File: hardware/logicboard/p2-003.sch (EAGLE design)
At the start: 67 parts, among them IC1 74LS06N, IC11 74LS153D, IC12 LTC485S, IC13 LTC485S, IC2 4066N, J1 MKR, J11 Qwiic, J12 Qwiic, J13 Qwiic, J14 Qwiic, J2 GPIO, J3 Vcc, J4 RLY, J5 SPI, J6 LED, K1 G5V1, T1 2SC1815, U1 DS18B20

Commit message: Very rough but should be okay.
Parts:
- removed C11, C12, C13: 10n, rcl:C-EUC2012
- removed IC11: 74LS153D, 74xx-us:74LS153D
- removed IC12, IC13: LTC485S, linear-technology:LTC485S
- removed IN, RX: (no value), wirepad:SMD2
- removed J11, J12, J13, J14: Qwiic, SparkFun-Connectors:QWIIC_CONNECTORJS-1MM
- removed J6: LED, SparkFun-Connectors:CONN_03JST-PTH
- removed JP3: MPXJMP, pinhead:PINHD-1X2
- removed JP5: D5V, pinhead:PINHD-1X3
- removed JP6: LED, pinhead:PINHD-1X3
- removed R11: 10k, rcl:R-EU_M2012
- removed R12, R13: 120, rcl:R-EU_M2012
- removed R3, R4: 120, resistor:R-EU_0204/5
- added J10: (no value), con-jack:JACK-PLUG0
- added J7, J8, J9: DIN5, SparkFun-Connectors:DIN5
- added X3: MKDSN1,5/2-5,08, con-phoenix-508:MKDSN1,5/2-5,08
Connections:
- removed net LED0A: J6.1, JP6.1, R4.1
- removed net LED1A: J6.3, JP6.3, R3.1
- removed net MIN: IC11A.1C1, IN.P, JP3.2, OK1A.VO1
- removed net MRX: IC11A.1C0, IC12.RO
- net GND: now also X3-1.KL; no longer C11.2, C12.2, C13.2, IC11A.1C2, IC11A.1C3, IC11A.1G, IC11A.2C0, IC11A.2C1, IC11A.2C2, IC11A.2C3, IC11A.2G, IC11A.B, IC12.!RE, IC12.DE, IC12.DI, IC12.GND, IC13.GND, J11.GND, J12.GND, J13.GND, J14.GND, J6.2, JP5.1, JP6.2
- net LED0: no longer R4.2
- net LED1: no longer R3.2
- net MRX+: no longer IC12.A, R12.1
- net MRX-: no longer IC12.B, R12.2
- net MRXDTCT: no longer IC11A.A, R11.1
- net MTX+: no longer IC13.A, R13.1
- net MTX-: no longer IC13.B, R13.2
- net RX: now also OK1A.VO1; no longer IC11A.1Y, JP3.1, RX.P
- net SCL: no longer J11.SCL, J12.SCL, J13.SCL, J14.SCL
- net SDA: no longer J11.SDA, J12.SDA, J13.SDA, J14.SDA
- net TX: no longer IC13.DI
- net V+: now also X3-2.KL; no longer JP5.3
- net VCC: no longer C11.1, C12.1, C13.1, IC12.VCC, IC13.!RE, IC13.DE, IC13.VCC, J11.VCC, J12.VCC, J13.VCC, J14.VCC, JP5.2, R11.2

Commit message: Configuring.
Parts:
- added JP3: (no value), pinhead:PINHD-1X3
- added JP5: (no value), pinhead:PINHD-1X2
- added R3, R4: 1k, resistor:R-EU_0204/5
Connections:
- new net LED0A: JP3.3, R3.1
- new net LED1A: JP3.1, R4.1
- net GND: now also JP3.2
- net LED0: now also R3.2
- net LED1: now also R4.2
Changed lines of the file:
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@@
 <part name="J10" library="con-jack" library_urn="urn:adsk.eagle:library:154" deviceset="JACK-PLUG" device="0" package3d_urn="urn:adsk.eagle:package:7492/1"/>
 <part name="X3" library="con-phoenix-508" library_urn="urn:adsk.eagle:library:176" deviceset="MKDSN1,5/2-5,08" device="" package3d_urn="urn:adsk.eagle:package:9630/1"/>
+<part name="R3" library="resistor" library_urn="urn:adsk.eagle:library:348" deviceset="R-EU_" device="0204/5" package3d_urn="urn:adsk.eagle:package:23488/1" value="1k"/>
+<part name="R4" library="resistor" library_urn="urn:adsk.eagle:library:348" deviceset="R-EU_" device="0204/5" package3d_urn="urn:adsk.eagle:package:23488/1" value="1k"/>
+<part name="JP3" library="pinhead" library_urn="urn:adsk.eagle:library:325" deviceset="PINHD-1X3" device="" package3d_urn="urn:adsk.eagle:package:22458/2"/>
+<part name="JP5" library="pinhead" library_urn="urn:adsk.eagle:library:325" deviceset="PINHD-1X2" device="" package3d_urn="urn:adsk.eagle:package:22435/2"/>
 </parts>
 <sheets>
@@
 <attribute name="VALUE" x="342.9" y="49.657" size="1.778" layer="96" rot="MR0"/>
 </instance>
+<instance part="R3" gate="G$1" x="93.98" y="33.02" smashed="yes">
+<attribute name="NAME" x="93.98" y="35.56" size="1.778" layer="95" align="bottom-center"/>
+<attribute name="VALUE" x="93.98" y="30.48" size="1.778" layer="96" align="top-center"/>
+</instance>
+<instance part="R4" gate="G$1" x="93.98" y="38.1" smashed="yes">
+<attribute name="NAME" x="93.98" y="40.64" size="1.778" layer="95" align="bottom-center"/>
+<attribute name="VALUE" x="93.98" y="35.56" size="1.778" layer="96" align="top-center"/>
+</instance>
+<instance part="JP3" gate="A" x="71.12" y="35.56" smashed="yes" rot="MR0">
+<attribute name="NAME" x="77.47" y="41.275" size="1.778" layer="95" rot="MR0"/>
+<attribute name="VALUE" x="77.47" y="27.94" size="1.778" layer="96" rot="MR0"/>
+</instance>
+<instance part="JP5" gate="G$1" x="30.48" y="165.1" smashed="yes" rot="MR0">
+<attribute name="NAME" x="36.83" y="170.815" size="1.778" layer="95" rot="MR0"/>
+<attribute name="VALUE" x="36.83" y="160.02" size="1.778" layer="96" rot="MR0"/>
+</instance>
 </instances>
 <busses>
@@
 <junction x="78.74" y="35.56"/>
 <wire x1="78.74" y1="20.32" x2="66.04" y2="20.32" width="0.1524" layer="91"/>
+<pinref part="JP3" gate="A" pin="2"/>
 </segment>
 <segment>
@@
 <wire x1="312.42" y1="91.44" x2="309.88" y2="91.44" width="0.1524" layer="91"/>
 <label x="309.88" y="91.44" size="0.8128" layer="95" rot="MR0" xref="yes"/>
-</segment>
-<segment>
-<wire x1="35.56" y1="162.56" x2="43.18" y2="162.56" width="0.1524" layer="91"/>
-<label x="43.18" y="162.56" size="0.8128" layer="95" xref="yes"/>
 </segment>
 <segment>
@@
 </segment>
 <segment>
-<wire x1="35.56" y1="165.1" x2="43.18" y2="165.1" width="0.1524" layer="91"/>
-<label x="43.18" y="165.1" size="0.8128" layer="95" xref="yes"/>
-</segment>
-<segment>
 <wire x1="96.52" y1="66.04" x2="101.6" y2="66.04" width="0.1524" layer="91"/>
 <pinref part="J3" gate="G$1" pin="2"/>
@@
 <wire x1="99.06" y1="33.02" x2="101.6" y2="33.02" width="0.1524" layer="91"/>
 <label x="101.6" y="33.02" size="0.8128" layer="95" xref="yes"/>
+<pinref part="R3" gate="G$1" pin="2"/>
 </segment>
 <segment>
@@
 <wire x1="99.06" y1="38.1" x2="101.6" y2="38.1" width="0.1524" layer="91"/>
 <label x="101.6" y="38.1" size="0.8128" layer="95" xref="yes"/>
+<pinref part="R4" gate="G$1" pin="2"/>
 </segment>
 </net>
@@
 <wire x1="76.2" y1="22.86" x2="66.04" y2="22.86" width="0.1524" layer="91"/>
 <label x="81.28" y="38.1" size="1.778" layer="95"/>
+<pinref part="R4" gate="G$1" pin="1"/>
+<pinref part="JP3" gate="A" pin="1"/>
 </segment>
 </net>
@@
 </segment>
 <segment>
-<wire x1="35.56" y1="167.64" x2="43.18" y2="167.64" width="0.1524" layer="91"/>
-<label x="43.18" y="167.64" size="0.8128" layer="95" xref="yes"/>
-</segment>
-<segment>
 <pinref part="SV2" gate="-2" pin="S"/>
 <wire x1="312.42" y1="157.48" x2="309.88" y2="157.48" width="0.1524" layer="91"/>
@@
 <junction x="81.28" y="33.02"/>
 <label x="81.28" y="33.02" size="1.778" layer="95"/>
-</segment>
-</net>
+<pinref part="R3" gate="G$1" pin="1"/>
+<pinref part="JP3" gate="A" pin="3"/>
+</segment>
+</net>

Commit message: First try. Should work. Need to renumber and rename parts.
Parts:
- removed C10: 100n, rcl:C-EU025-024X044
- removed C8, C9: 10n, resistor:C-EU025-024X044
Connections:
- net GND: no longer C10.2, C8.2, C9.2
- net VCC: no longer C10.1, C8.1, C9.1

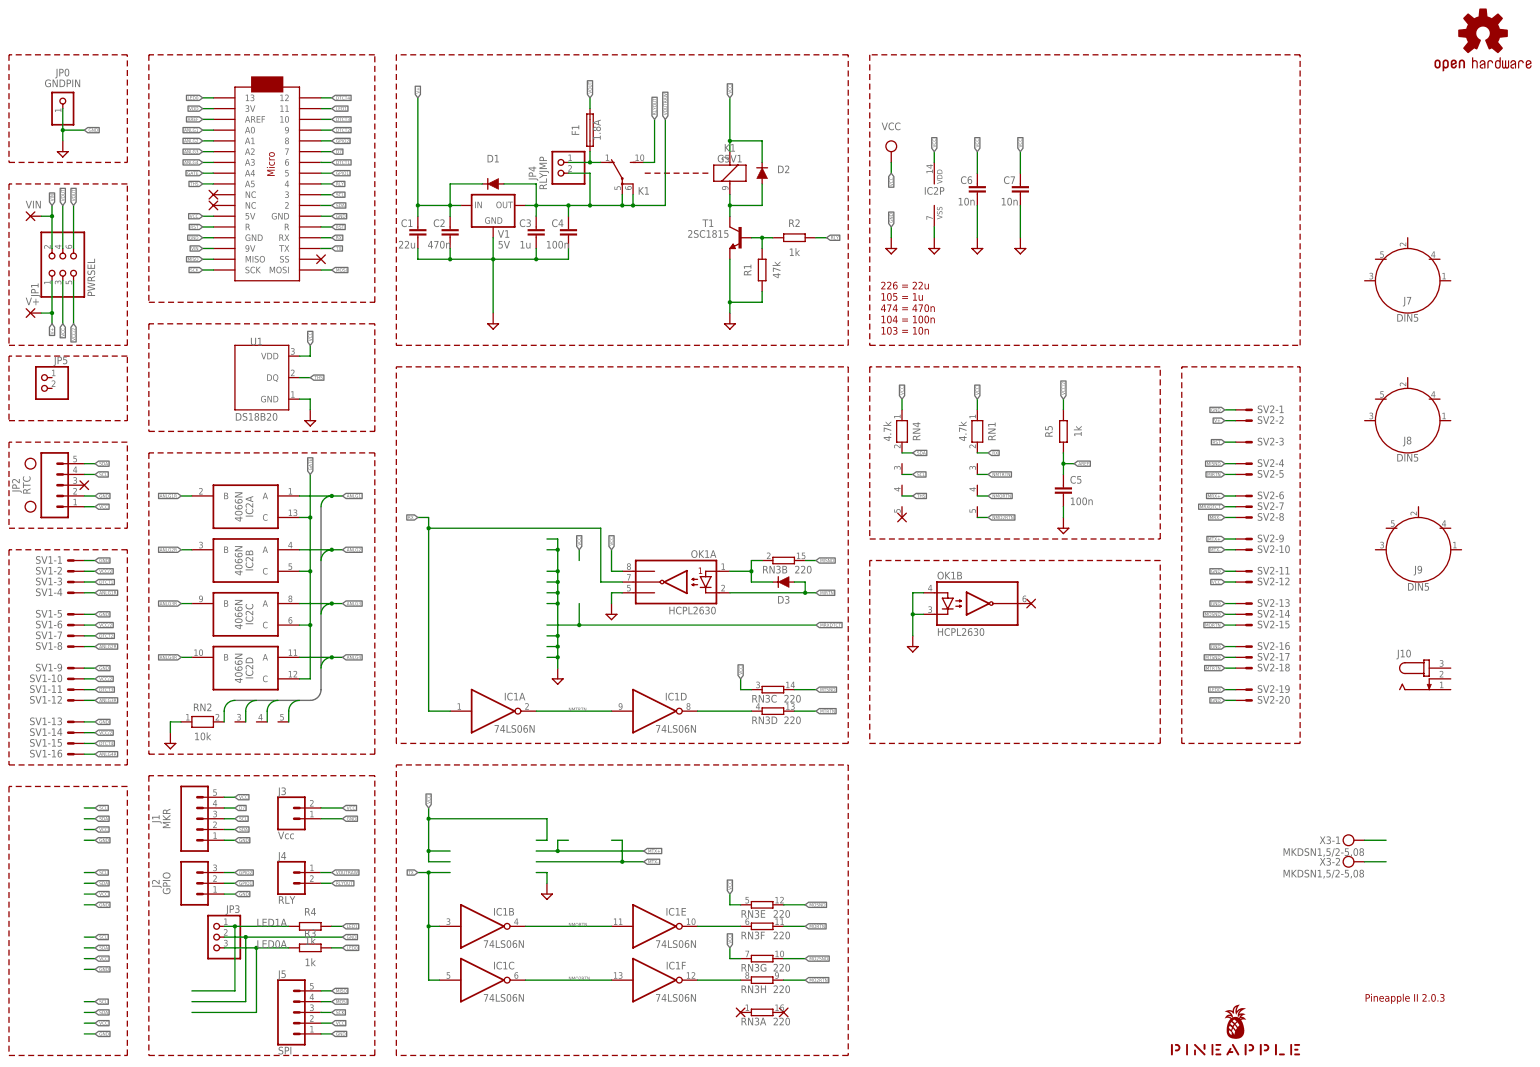
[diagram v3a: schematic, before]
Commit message: Renumbered some connectors.
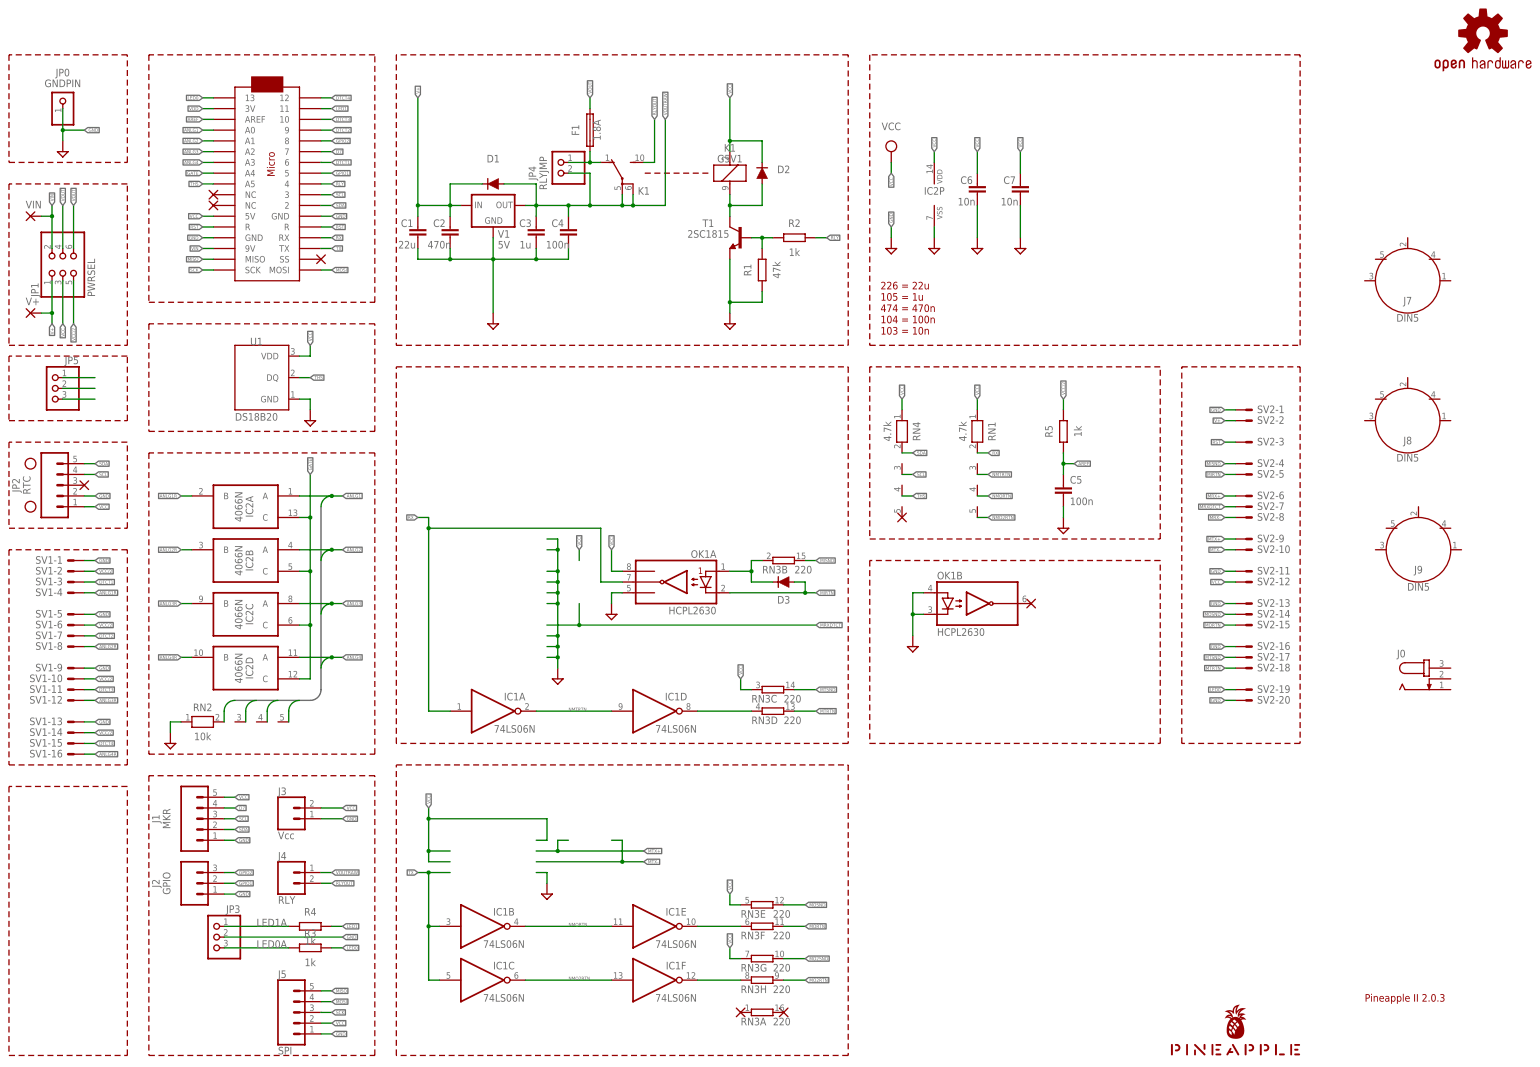
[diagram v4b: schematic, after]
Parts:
- removed X3: MKDSN1,5/2-5,08, con-phoenix-508:MKDSN1,5/2-5,08
- JP5: device pinhead:PINHD-1X2 -> pinhead:PINHD-1X3
- renumbered J10 to J0
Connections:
- net GND: now also JP5.1; no longer X3-1.KL
- net V+: now also JP5.3; no longer X3-2.KL
- net VCC: now also JP5.2
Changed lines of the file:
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@@
 <part name="J8" library="SparkFun-Connectors" library_urn="urn:adsk.eagle:library:513" deviceset="DIN5" device="" package3d_urn="urn:adsk.eagle:package:38294/1"/>
 <part name="J9" library="SparkFun-Connectors" library_urn="urn:adsk.eagle:library:513" deviceset="DIN5" device="" package3d_urn="urn:adsk.eagle:package:38294/1"/>
-<part name="J10" library="con-jack" library_urn="urn:adsk.eagle:library:154" deviceset="JACK-PLUG" device="0" package3d_urn="urn:adsk.eagle:package:7492/1"/>
-<part name="X3" library="con-phoenix-508" library_urn="urn:adsk.eagle:library:176" deviceset="MKDSN1,5/2-5,08" device="" package3d_urn="urn:adsk.eagle:package:9630/1"/>
+<part name="J0" library="con-jack" library_urn="urn:adsk.eagle:library:154" deviceset="JACK-PLUG" device="0" package3d_urn="urn:adsk.eagle:package:7492/1"/>
 <part name="R3" library="resistor" library_urn="urn:adsk.eagle:library:348" deviceset="R-EU_" device="0204/5" package3d_urn="urn:adsk.eagle:package:23488/1" value="1k"/>
 <part name="R4" library="resistor" library_urn="urn:adsk.eagle:library:348" deviceset="R-EU_" device="0204/5" package3d_urn="urn:adsk.eagle:package:23488/1" value="1k"/>
 <part name="JP3" library="pinhead" library_urn="urn:adsk.eagle:library:325" deviceset="PINHD-1X3" device="" package3d_urn="urn:adsk.eagle:package:22458/2"/>
-<part name="JP5" library="pinhead" library_urn="urn:adsk.eagle:library:325" deviceset="PINHD-1X2" device="" package3d_urn="urn:adsk.eagle:package:22435/2"/>
+<part name="JP5" library="pinhead" library_urn="urn:adsk.eagle:library:325" deviceset="PINHD-1X3" device="" package3d_urn="urn:adsk.eagle:package:22458/2"/>
 </parts>
 <sheets>
@@
 <attribute name="VALUE" x="355.6" y="119.126" size="1.778" layer="96" font="vector" align="top-center"/>
 </instance>
-<instance part="J10" gate="G$1" x="358.14" y="96.52" smashed="yes">
+<instance part="J0" gate="G$1" x="358.14" y="96.52" smashed="yes">
 <attribute name="NAME" x="350.52" y="101.6" size="1.778" layer="95"/>
 <attribute name="VALUE" x="350.52" y="91.44" size="1.778" layer="96"/>
-</instance>
-<instance part="X3" gate="-1" x="340.36" y="58.42" smashed="yes" rot="MR0">
-<attribute name="NAME" x="337.312" y="57.531" size="1.778" layer="95" rot="MR0"/>
-<attribute name="VALUE" x="342.9" y="54.737" size="1.778" layer="96" rot="MR0"/>
-</instance>
-<instance part="X3" gate="-2" x="340.36" y="53.34" smashed="yes" rot="MR0">
-<attribute name="NAME" x="337.312" y="52.451" size="1.778" layer="95" rot="MR0"/>
-<attribute name="VALUE" x="342.9" y="49.657" size="1.778" layer="96" rot="MR0"/>
 </instance>
 <instance part="R3" gate="G$1" x="93.98" y="33.02" smashed="yes">
@@
 <attribute name="VALUE" x="77.47" y="27.94" size="1.778" layer="96" rot="MR0"/>
 </instance>
-<instance part="JP5" gate="G$1" x="30.48" y="165.1" smashed="yes" rot="MR0">
-<attribute name="NAME" x="36.83" y="170.815" size="1.778" layer="95" rot="MR0"/>
-<attribute name="VALUE" x="36.83" y="160.02" size="1.778" layer="96" rot="MR0"/>
+<instance part="JP5" gate="A" x="33.02" y="165.1" smashed="yes" rot="MR0">
+<attribute name="NAME" x="39.37" y="170.815" size="1.778" layer="95" rot="MR0"/>
+<attribute name="VALUE" x="39.37" y="157.48" size="1.778" layer="96" rot="MR0"/>
 </instance>
 </instances>
@@
 </segment>
 <segment>
-<wire x1="40.64" y1="58.42" x2="43.18" y2="58.42" width="0.1524" layer="91"/>
-<label x="43.18" y="58.42" size="0.8128" layer="95" xref="yes"/>
-</segment>
-<segment>
-<wire x1="40.64" y1="43.18" x2="43.18" y2="43.18" width="0.1524" layer="91"/>
-<label x="43.18" y="43.18" size="0.8128" layer="95" xref="yes"/>
-</segment>
-<segment>
-<wire x1="40.64" y1="12.7" x2="43.18" y2="12.7" width="0.1524" layer="91"/>
-<label x="43.18" y="12.7" size="0.8128" layer="95" xref="yes"/>
-</segment>
-<segment>
 <pinref part="J2" gate="J$1" pin="1"/>
 <wire x1="73.66" y1="45.72" x2="76.2" y2="45.72" width="0.1524" layer="91"/>
@@
 </segment>
 <segment>
-<wire x1="40.64" y1="27.94" x2="43.18" y2="27.94" width="0.1524" layer="91"/>
-<label x="43.18" y="27.94" size="0.8128" layer="95" xref="yes"/>
-</segment>
-<segment>
 <label x="101.6" y="35.56" size="0.8128" layer="95" xref="yes"/>
-<wire x1="73.66" y1="35.56" x2="78.74" y2="35.56" width="0.1524" layer="91"/>
-<wire x1="78.74" y1="35.56" x2="101.6" y2="35.56" width="0.1524" layer="91"/>
-<wire x1="78.74" y1="35.56" x2="78.74" y2="20.32" width="0.1524" layer="91"/>
-<junction x="78.74" y="35.56"/>
-<wire x1="78.74" y1="20.32" x2="66.04" y2="20.32" width="0.1524" layer="91"/>
+<wire x1="73.66" y1="35.56" x2="101.6" y2="35.56" width="0.1524" layer="91"/>
 <pinref part="JP3" gate="A" pin="2"/>
 </segment>
@@
 </segment>
 <segment>
-<pinref part="X3" gate="-1" pin="KL"/>
-<wire x1="342.9" y1="58.42" x2="347.98" y2="58.42" width="0.1524" layer="91"/>
+<pinref part="JP5" gate="A" pin="1"/>
+<wire x1="35.56" y1="167.64" x2="43.18" y2="167.64" width="0.1524" layer="91"/>
 </segment>
 </net>
@@
 <wire x1="40.64" y1="137.16" x2="43.18" y2="137.16" width="0.1524" layer="91"/>
 <label x="43.18" y="137.16" size="0.8128" layer="95" xref="yes"/>
-</segment>
-<segment>
-<wire x1="40.64" y1="60.96" x2="43.18" y2="60.96" width="0.1524" layer="91"/>
-<label x="43.18" y="60.96" size="0.8128" layer="95" xref="yes"/>
-</segment>
-<segment>
-<wire x1="40.64" y1="45.72" x2="43.18" y2="45.72" width="0.1524" layer="91"/>
-<label x="43.18" y="45.72" size="0.8128" layer="95" xref="yes"/>
-</segment>
-<segment>
-<wire x1="40.64" y1="30.48" x2="43.18" y2="30.48" width="0.1524" layer="91"/>
-<label x="43.18" y="30.48" size="0.8128" layer="95" xref="yes"/>
-</segment>
-<segment>
-<wire x1="40.64" y1="15.24" x2="43.18" y2="15.24" width="0.1524" layer="91"/>
-<label x="43.18" y="15.24" size="0.8128" layer="95" xref="yes"/>
 </segment>
 <segment>
@@
 <label x="309.88" y="119.38" size="0.8128" layer="95" rot="MR0" xref="yes"/>
 </segment>
+<segment>
+<pinref part="JP5" gate="A" pin="2"/>
+<wire x1="35.56" y1="165.1" x2="43.18" y2="165.1" width="0.1524" layer="91"/>
+</segment>
 </net>
 <net name="MIDIINSND" class="0">
@@
 </segment>
 <segment>
-<wire x1="40.64" y1="63.5" x2="43.18" y2="63.5" width="0.1524" layer="91"/>
-<label x="43.18" y="63.5" size="0.8128" layer="95" xref="yes"/>
-</segment>
-<segment>
-<wire x1="40.64" y1="48.26" x2="43.18" y2="48.26" width="0.1524" layer="91"/>
-<label x="43.18" y="48.26" size="0.8128" layer="95" xref="yes"/>
-</segment>
-<segment>
-<wire x1="40.64" y1="33.02" x2="43.18" y2="33.02" width="0.1524" layer="91"/>
-<label x="43.18" y="33.02" size="0.8128" layer="95" xref="yes"/>
-</segment>
-<segment>
-<wire x1="40.64" y1="17.78" x2="43.18" y2="17.78" width="0.1524" layer="91"/>
-<label x="43.18" y="17.78" size="0.8128" layer="95" xref="yes"/>
-</segment>
-<segment>
 <pinref part="RN4" gate="1" pin="2"/>
 <wire x1="233.68" y1="149.86" x2="236.22" y2="149.86" width="0.1524" layer="91"/>
@@
 <wire x1="40.64" y1="144.78" x2="43.18" y2="144.78" width="0.1524" layer="91"/>
 <label x="43.18" y="144.78" size="0.8128" layer="95" xref="yes"/>
-</segment>
-<segment>
-<wire x1="40.64" y1="66.04" x2="43.18" y2="66.04" width="0.1524" layer="91"/>
-<label x="43.18" y="66.04" size="0.8128" layer="95" xref="yes"/>
-</segment>
-<segment>
-<wire x1="40.64" y1="50.8" x2="43.18" y2="50.8" width="0.1524" layer="91"/>
-<label x="43.18" y="50.8" size="0.8128" layer="95" xref="yes"/>
-</segment>
-<segment>
-<wire x1="40.64" y1="35.56" x2="43.18" y2="35.56" width="0.1524" layer="91"/>
-<label x="43.18" y="35.56" size="0.8128" layer="95" xref="yes"/>
-</segment>
-<segment>
-<wire x1="40.64" y1="20.32" x2="43.18" y2="20.32" width="0.1524" layer="91"/>
-<label x="43.18" y="20.32" size="0.8128" layer="95" xref="yes"/>
 </segment>
 <segment>
@@
 <net name="LED1A" class="0">
 <segment>
-<wire x1="88.9" y1="38.1" x2="76.2" y2="38.1" width="0.1524" layer="91"/>
-<wire x1="76.2" y1="38.1" x2="73.66" y2="38.1" width="0.1524" layer="91"/>
-<wire x1="76.2" y1="22.86" x2="76.2" y2="38.1" width="0.1524" layer="91"/>
-<junction x="76.2" y="38.1"/>
-<wire x1="76.2" y1="22.86" x2="66.04" y2="22.86" width="0.1524" layer="91"/>
+<wire x1="88.9" y1="38.1" x2="73.66" y2="38.1" width="0.1524" layer="91"/>
 <label x="81.28" y="38.1" size="1.778" layer="95"/>
 <pinref part="R4" gate="G$1" pin="1"/>
@@
 </segment>
 <segment>
-<pinref part="X3" gate="-2" pin="KL"/>
-<wire x1="342.9" y1="53.34" x2="347.98" y2="53.34" width="0.1524" layer="91"/>
+<pinref part="JP5" gate="A" pin="3"/>
+<wire x1="35.56" y1="162.56" x2="43.18" y2="162.56" width="0.1524" layer="91"/>
 </segment>
 </net>
 <net name="LED0A" class="0">
 <segment>
-<wire x1="81.28" y1="17.78" x2="66.04" y2="17.78" width="0.1524" layer="91"/>
-<wire x1="88.9" y1="33.02" x2="81.28" y2="33.02" width="0.1524" layer="91"/>
-<wire x1="81.28" y1="33.02" x2="73.66" y2="33.02" width="0.1524" layer="91"/>
-<wire x1="81.28" y1="17.78" x2="81.28" y2="33.02" width="0.1524" layer="91"/>
-<junction x="81.28" y="33.02"/>
+<wire x1="88.9" y1="33.02" x2="73.66" y2="33.02" width="0.1524" layer="91"/>
 <label x="81.28" y="33.02" size="1.778" layer="95"/>
 <pinref part="R3" gate="G$1" pin="1"/>
